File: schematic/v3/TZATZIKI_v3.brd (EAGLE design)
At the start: 41 x 50 mm, 8 parts, among them J1 2X20-CHIP-HEADERS2X20CHIP_OFF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

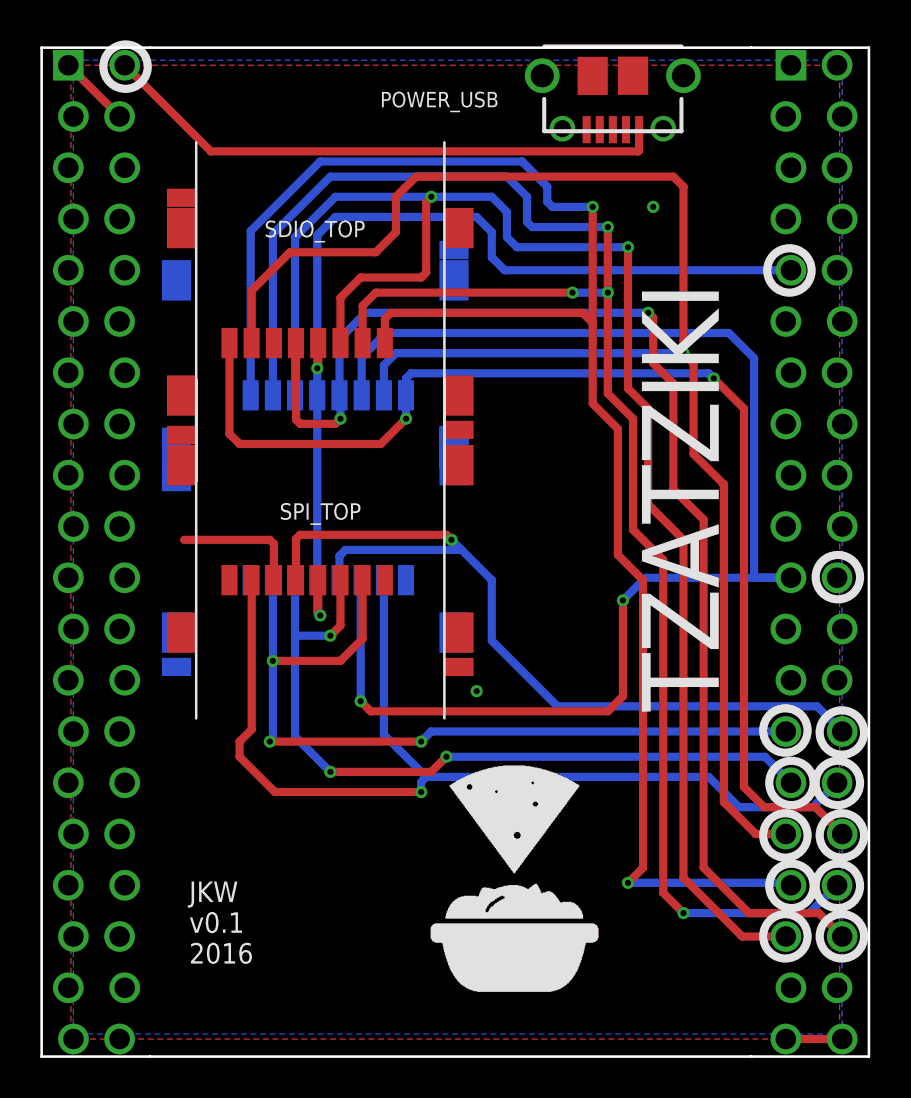
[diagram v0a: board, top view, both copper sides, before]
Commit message: added v4 with card detect pin
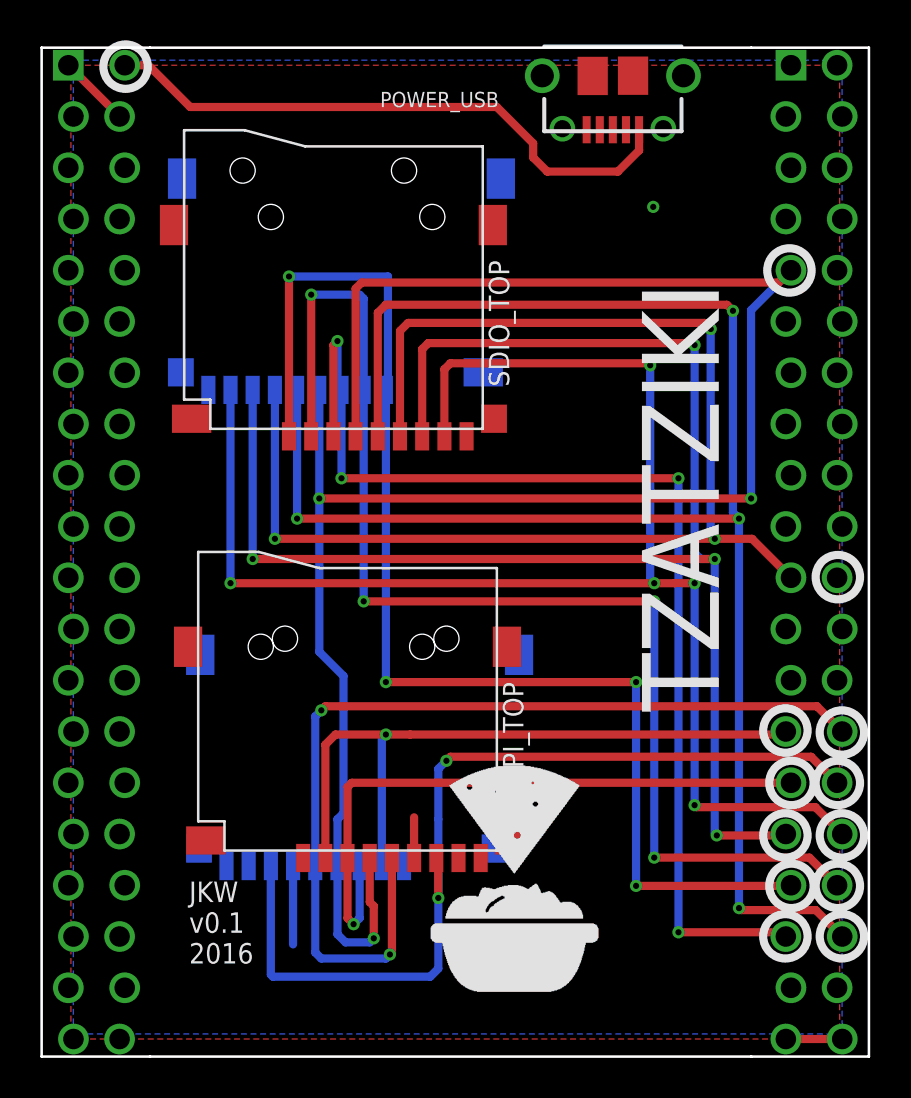
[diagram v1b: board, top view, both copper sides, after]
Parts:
- SDIO_BOT, SDIO_TOP, SPI_BOT, SPI_TOP: value USD-SDIO-SOCKET -> TF-HOLDER; device JKW_CHIP:MICRO-SD-SOCKET-SDIO -> JKW_CHIP:TF-PULL
- moved SPI_BOT 7.62 mm to (23.2, 32.7)
- moved SDIO_BOT 7.26 mm to (22.3, 56.3)
- moved SPI_TOP 7.03 mm to (22.6, 33.1)
- moved SDIO_TOP 2.34 mm to (21.9, 54.0)
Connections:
- new net N$16: J1.CSID7, SDIO_BOT.9, SDIO_TOP.9, SPI_BOT.9, SPI_TOP.9
- net GND: now also SDIO_BOT.6, SDIO_BOT.S1, SDIO_BOT.S2, SDIO_BOT.S3, SDIO_BOT.S4, SDIO_TOP.6, SDIO_TOP.S1, SDIO_TOP.S2, SDIO_TOP.S3, SDIO_TOP.S4, SPI_BOT.6, SPI_BOT.S1, SPI_BOT.S2, SPI_BOT.S3, SPI_BOT.S4, SPI_TOP.6, SPI_TOP.S1, SPI_TOP.S2, SPI_TOP.S3, SPI_TOP.S4; no longer SDIO_BOT.CD1, SDIO_BOT.CD2, SDIO_BOT.GND, SDIO_BOT.GND1, SDIO_BOT.GND3, SDIO_BOT.GND@1, SDIO_BOT.GND@2, SDIO_TOP.CD1, SDIO_TOP.CD2, SDIO_TOP.GND, SDIO_TOP.GND1, SDIO_TOP.GND3, SDIO_TOP.GND@1, SDIO_TOP.GND@2, SPI_BOT.CD1, SPI_BOT.CD2, SPI_BOT.GND, SPI_BOT.GND1, SPI_BOT.GND3, SPI_BOT.GND@1, SPI_BOT.GND@2, SPI_TOP.CD1, SPI_TOP.CD2, SPI_TOP.GND, SPI_TOP.GND1, SPI_TOP.GND3, SPI_TOP.GND@1, SPI_TOP.GND@2
- net N$10: now also SDIO_BOT.4, SDIO_TOP.4, SPI_BOT.4, SPI_TOP.4; no longer SDIO_BOT.VDD, SDIO_TOP.VDD, SPI_BOT.VDD, SPI_TOP.VDD
- net N$11: now also SPI_BOT.2, SPI_TOP.2; no longer SPI_BOT.CD/DAT3, SPI_TOP.CD/DAT3
- net N$12: now also SPI_BOT.3, SPI_TOP.3; no longer SPI_BOT.CMD, SPI_TOP.CMD
- net N$13: now also SPI_BOT.7, SPI_TOP.7; no longer SPI_BOT.DAT0, SPI_TOP.DAT0
- net N$14: now also SPI_BOT.5, SPI_TOP.5; no longer SPI_BOT.CLK, SPI_TOP.CLK
- net N$2: now also SDIO_BOT.2, SDIO_TOP.2; no longer SDIO_BOT.CD/DAT3, SDIO_TOP.CD/DAT3
- net N$3: now also SDIO_BOT.7, SDIO_TOP.7; no longer SDIO_BOT.DAT0, SDIO_TOP.DAT0
- net N$4: now also SDIO_BOT.3, SDIO_TOP.3; no longer SDIO_BOT.CMD, SDIO_TOP.CMD
- net N$5: now also SDIO_BOT.5, SDIO_TOP.5; no longer SDIO_BOT.CLK, SDIO_TOP.CLK
- net N$6: now also SDIO_BOT.8, SDIO_TOP.8; no longer SDIO_BOT.DAT1, SDIO_TOP.DAT1
- net N$9: now also SDIO_BOT.1, SDIO_TOP.1; no longer SDIO_BOT.DAT2, SDIO_TOP.DAT2
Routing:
- net N$10: track 48.0 -> 96.7 mm, vias 2 -> 3
- net N$5: track 62.9 -> 87.7 mm, vias 2 -> 4
- net N$2: track 85.5 -> 61.4 mm
- net N$4: track 76.5 -> 56.3 mm, vias 2 -> 4
- net N$9: track 82.7 -> 63.2 mm, vias 2 -> 4
- net N$6: track 58.1 -> 76.1 mm, vias 2 -> 5
- net N$12: track 38.6 -> 32.0 mm, vias 3 -> 1
- net N$11: track 41.6 -> 35.3 mm, vias 3 -> 1
- net N$13: track 51.7 -> 46.4 mm, vias 1 -> 2
- net N$14: track 42.4 -> 47.3 mm, vias 1 -> 2
- net GND: track 80.8 -> 77.4 mm
- net N$3: track 79.2 -> 77.9 mm, vias 1 -> 4
- net VOUT: track 28.3 -> 29.5 mm
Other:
- board text added: "Not Ordered"
